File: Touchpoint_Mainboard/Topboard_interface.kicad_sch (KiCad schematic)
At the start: 1 part, among them J3 Conn_01x10

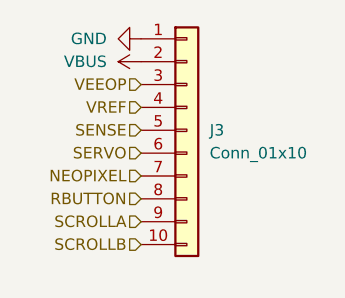
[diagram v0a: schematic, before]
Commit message: FInished populating mainboard schematic
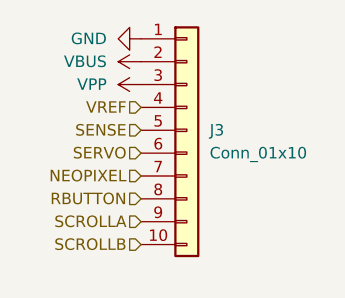
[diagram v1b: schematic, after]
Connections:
- net VEEOP renamed VPP
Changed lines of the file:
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@@
-		)
-	)
-	(hierarchical_label "VEEOP"
-		(shape input)
-		(at 52.07 43.18 180)
-		(effects
-			(font
-				(size 1.27 1.27)
-			)
-			(justify right)
 		)
 	)
@@
 					(unit 1)
 				)
+			)
+		)
+	)
+	(symbol
+		(lib_id "power:VPP")
+		(at 52.07 43.18 90)
+		(unit 1)
+		(exclude_from_sim no)
+		(in_bom yes)
+		(on_board yes)
+		(dnp no)
+		(fields_autoplaced yes)
+		(property "Reference" "#PWR081"
+			(at 55.88 43.18 0)
+			(effects
+				(font
+					(size 1.27 1.27)
+				)
+				(hide yes)
+			)
+		)
+		(property "Value" "VPP"
+			(at 48.26 43.1799 90)
+			(effects
+				(font
+					(size 1.27 1.27)
+				)
+				(justify left)
+			)
+		)
+		(property "Footprint" ""
+			(at 52.07 43.18 0)
+			(effects
+				(font
+					(size 1.27 1.27)
+				)
+				(hide yes)
+			)
+		)
+		(property "Datasheet" ""
+			(at 52.07 43.18 0)
+			(effects
+				(font
+					(size 1.27 1.27)
+				)
+				(hide yes)
+			)
+		)
+		(property "Description" "Power symbol creates a global label with name \"VPP\""
+			(at 52.07 43.18 0)
+			(effects
+				(font
+					(size 1.27 1.27)
+				)
+				(hide yes)
+			)
+		)
+		(pin "1"
+		)
+		(instances
+			(project "Touchpoint_Mainboard"
+				(path "/f37b5f88-420a-4646-85df-8f9851d23e3c/3f8a48d9-15ab-478a-aaa5-794276ddae05"
+					(reference "#PWR081")
+					(unit 1)
+				)

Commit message: Added remaining interface things to topboard schematic
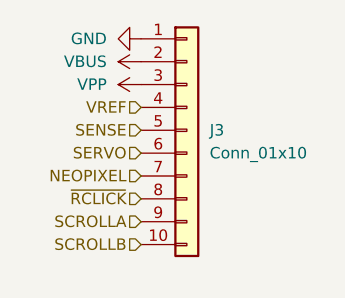
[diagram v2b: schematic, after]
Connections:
- net RBUTTON renamed ~{RCLICK}
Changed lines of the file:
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@@
 		)
 	)
-	(hierarchical_label "RBUTTON"
+	(hierarchical_label "~{RCLICK}"
 		(shape input)
 		(at 52.07 55.88 180)

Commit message: Finished assigning most footprints
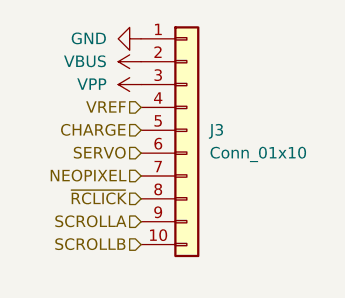
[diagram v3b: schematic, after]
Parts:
- J3: footprint (none) -> Connector_PinHeader_2.54mm:PinHeader_1x10_P2.54mm_Vertical
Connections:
- net SENSE renamed CHARGE
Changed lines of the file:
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@@
 		)
 	)
-	(hierarchical_label "SENSE"
+	(hierarchical_label "CHARGE"
 		(shape input)
 		(at 52.07 48.26 180)
@@
 			)
 		)
-		(property "Footprint" ""
+		(property "Footprint" "Connector_PinHeader_2.54mm:PinHeader_1x10_P2.54mm_Vertical"
 			(at 57.15 48.26 0)
 			(effects

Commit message: Changed to jumper connector between boards
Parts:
- J3: footprint Connector_PinHeader_2.54mm:PinHeader_1x10_P2.54mm_Vertical -> Touchpoint:Jumper_Interface_10
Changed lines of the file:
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@@
 			)
 		)
-		(property "Footprint" "Connector_PinHeader_2.54mm:PinHeader_1x10_P2.54mm_Vertical"
+		(property "Footprint" "Touchpoint:Jumper_Interface_10"
 			(at 57.15 48.26 0)
 			(effects

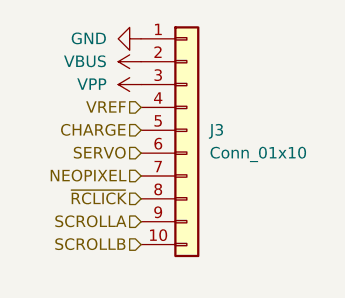
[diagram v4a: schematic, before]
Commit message: Added 3.3V to interface
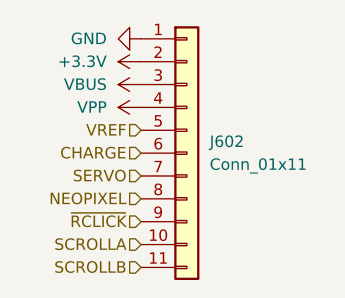
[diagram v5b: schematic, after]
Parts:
- removed J3: Conn_01x10, Touchpoint:Jumper_Interface_10, symbol Connector_Generic:Conn_01x10
- added J602: Conn_01x11, Touchpoint:Jumper_Interface_11, symbol Connector_Generic:Conn_01x11
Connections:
- net CHARGE: now also J602.6 (Pin_6)
- net GND: now also J602.1 (Pin_1)
- net NEOPIXEL: now also J602.8 (Pin_8)
- net SCROLLA: now also J602.10 (Pin_10)
- net SCROLLB: now also J602.11 (Pin_11)
- net SERVO: now also J602.7 (Pin_7)
- net VBUS: now also J602.3 (Pin_3)
- net VPP: now also J602.4 (Pin_4)
- net VREF: now also J602.5 (Pin_5)
- net ~{RCLICK}: now also J602.9 (Pin_9)
- new net +3.3V: J602.2 (Pin_2)
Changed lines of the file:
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@@
 	(hierarchical_label "SCROLLA"
 		(shape input)
+		(at 52.07 60.96 180)
+		(effects
+			(font
+				(size 1.27 1.27)
+			)
+			(justify right)
+		)
+	)
+	(hierarchical_label "VREF"
+		(shape input)
+		(at 52.07 48.26 180)
+		(effects
+			(font
+				(size 1.27 1.27)
+			)
+			(justify right)
+		)
+	)
+	(hierarchical_label "SERVO"
+		(shape input)
+		(at 52.07 53.34 180)
+		(effects
+			(font
+				(size 1.27 1.27)
+			)
+			(justify right)
+		)
+	)
+	(hierarchical_label "~{RCLICK}"
+		(shape input)
 		(at 52.07 58.42 180)
 		(effects
@@
 		)
 	)
-	(hierarchical_label "VREF"
-		(shape input)
-		(at 52.07 45.72 180)
-		(effects
-			(font
-				(size 1.27 1.27)
-			)
-			(justify right)
-		)
-	)
-	(hierarchical_label "SERVO"
+	(hierarchical_label "SCROLLB"
+		(shape input)
+		(at 52.07 63.5 180)
+		(effects
+			(font
+				(size 1.27 1.27)
+			)
+			(justify right)
+		)
+	)
+	(hierarchical_label "CHARGE"
 		(shape input)
 		(at 52.07 50.8 180)
@@
 		)
 	)
-	(hierarchical_label "~{RCLICK}"
+	(hierarchical_label "NEOPIXEL"
 		(shape input)
 		(at 52.07 55.88 180)
@@
 		)
 	)
-	(hierarchical_label "SCROLLB"
-		(shape input)
-		(at 52.07 60.96 180)
-		(effects
-			(font
-				(size 1.27 1.27)
-			)
-			(justify right)
-		)
-	)
-	(hierarchical_label "CHARGE"
-		(shape input)
-		(at 52.07 48.26 180)
-		(effects
-			(font
-				(size 1.27 1.27)
-			)
-			(justify right)
-		)
-	)
-	(hierarchical_label "NEOPIXEL"
-		(shape input)
-		(at 52.07 53.34 180)
-		(effects
-			(font
-				(size 1.27 1.27)
-			)
-			(justify right)
-		)
-	)
 	(symbol
-		(lib_id "Connector_Generic:Conn_01x10")
-		(at 57.15 48.26 0)
+		(lib_id "power:VBUS")
+		(at 52.07 43.18 90)
 		(unit 1)
 		(exclude_from_sim no)
@@
 		(dnp no)
 		(fields_autoplaced yes)
-		(property "Reference" "J3"
-			(at 59.69 48.2599 0)
+		(property "Reference" "#PWR0602"
+			(at 55.88 43.18 0)
+			(effects
+				(font
+					(size 1.27 1.27)
+				)
+				(hide yes)
+			)
+		)
+		(property "Value" "VBUS"
+			(at 48.26 43.1799 90)
 			(effects
 				(font
@@
 			)
 		)
-		(property "Value" "Conn_01x10"
-			(at 59.69 50.7999 0)
-			(effects
-				(font
-					(size 1.27 1.27)
-				)
-				(justify left)
-			)
-		)
-		(property "Footprint" "Touchpoint:Jumper_Interface_10"
-			(at 57.15 48.26 0)
-			(effects
-				(font
-					(size 1.27 1.27)
-				)
-				(hide yes)
-			)
-		)
-		(property "Datasheet" "~"
-			(at 57.15 48.26 0)
-			(effects
-				(font
-					(size 1.27 1.27)
-				)
-				(hide yes)
-			)
-		)
-		(property "Description" "Generic connector, single row, 01x10, script generated (kicad-library-utils/schlib/autogen/connector/)"
-			(at 57.15 48.26 0)
+		(property "Footprint" ""
+			(at 52.07 43.18 0)
+			(effects
+				(font
+					(size 1.27 1.27)
+				)
+				(hide yes)
+			)
+		)
+		(property "Datasheet" ""
+			(at 52.07 43.18 0)
+			(effects
+				(font
+					(size 1.27 1.27)
+				)
+				(hide yes)
+			)
+		)
+		(property "Description" "Power symbol creates a global label with name \"VBUS\""
+			(at 52.07 43.18 0)
 			(effects
 				(font
@@
 		)
 		(pin "1"
-		)
-		(pin "2"
-		)
-		(pin "3"
-		)
-		(pin "4"
-		)
-		(pin "5"
-		)
-		(pin "7"
-		)
-		(pin "9"
-		)
-		(pin "6"
-		)
-		(pin "8"
-		)
-		(pin "10"
 		)
 		(instances
 			(project ""
 				(path "/f37b5f88-420a-4646-85df-8f9851d23e3c/3f8a48d9-15ab-478a-aaa5-794276ddae05"
-					(reference "J3")
+					(reference "#PWR0602")
 					(unit 1)
 				)
@@
 	)
 	(symbol
-		(lib_id "power:VBUS")
+		(lib_id "power:+3.3V")
 		(at 52.07 40.64 90)
 		(unit 1)
@@
 		(dnp no)
 		(fields_autoplaced yes)
-		(property "Reference" "#PWR074"
+		(property "Reference" "#PWR0604"
 			(at 55.88 40.64 0)
 			(effects
@@
 			)
 		)
-		(property "Value" "VBUS"
+		(property "Value" "+3.3V"
 			(at 48.26 40.6399 90)
 			(effects
@@
 			)
 		)
-		(property "Description" "Power symbol creates a global label with name \"VBUS\""
+		(property "Description" "Power symbol creates a global label with name \"+3.3V\""
 			(at 52.07 40.64 0)
 			(effects
@@
 			(project ""
 				(path "/f37b5f88-420a-4646-85df-8f9851d23e3c/3f8a48d9-15ab-478a-aaa5-794276ddae05"
-					(reference "#PWR074")
+					(reference "#PWR0604")
 					(unit 1)
 				)
@@
 	(symbol
 		(lib_id "power:VPP")
-		(at 52.07 43.18 90)
+		(at 52.07 45.72 90)
 		(unit 1)
 		(exclude_from_sim no)
@@
 		(dnp no)
 		(fields_autoplaced yes)
-		(property "Reference" "#PWR081"
-			(at 55.88 43.18 0)
+		(property "Reference" "#PWR0603"
+			(at 55.88 45.72 0)
 			(effects
 				(font
@@
 		)
 		(property "Value" "VPP"
-			(at 48.26 43.1799 90)
+			(at 48.26 45.7199 90)
 			(effects
 				(font
@@
 		)
 		(property "Footprint" ""
-			(at 52.07 43.18 0)
+			(at 52.07 45.72 0)
 			(effects
 				(font
@@
 		)
 		(property "Datasheet" ""
-			(at 52.07 43.18 0)
+			(at 52.07 45.72 0)
 			(effects
 				(font
@@
 		)
 		(property "Description" "Power symbol creates a global label with name \"VPP\""
-			(at 52.07 43.18 0)
+			(at 52.07 45.72 0)
 			(effects
 				(font
@@
 			(project "Touchpoint_Mainboard"
 				(path "/f37b5f88-420a-4646-85df-8f9851d23e3c/3f8a48d9-15ab-478a-aaa5-794276ddae05"
-					(reference "#PWR081")
+					(reference "#PWR0603")
 					(unit 1)
 				)
@@
 		(dnp no)
 		(fields_autoplaced yes)
-		(property "Reference" "#PWR075"
+		(property "Reference" "#PWR0601"
 			(at 45.72 38.1 0)
 			(effects
@@
 			(project ""
 				(path "/f37b5f88-420a-4646-85df-8f9851d23e3c/3f8a48d9-15ab-478a-aaa5-794276ddae05"
-					(reference "#PWR075")
+					(reference "#PWR0601")
 					(unit 1)
 				)
+			)
+		)
+	)
+	(symbol
+		(lib_id "Connector_Generic:Conn_01x11")
+		(at 57.15 50.8 0)
+		(unit 1)
+		(exclude_from_sim no)
+		(in_bom yes)
+		(on_board yes)
+		(dnp no)
+		(fields_autoplaced yes)
+		(property "Reference" "J602"
+			(at 59.69 49.5299 0)
+			(effects
+				(font
+					(size 1.27 1.27)
+				)
+				(justify left)
+			)
+		)
+		(property "Value" "Conn_01x11"
+			(at 59.69 52.0699 0)
+			(effects
+				(font
+					(size 1.27 1.27)
+				)
+				(justify left)
+			)
+		)
+		(property "Footprint" "Touchpoint:Jumper_Interface_11"
+			(at 57.15 50.8 0)
+			(effects
+				(font
+					(size 1.27 1.27)
+				)
+				(hide yes)
+			)
+		)
+		(property "Datasheet" "~"
+			(at 57.15 50.8 0)
+			(effects
+				(font
+					(size 1.27 1.27)
+				)
+				(hide yes)
+			)
+		)
+		(property "Description" "Generic connector, single row, 01x11, script generated (kicad-library-utils/schlib/autogen/connector/)"
+			(at 57.15 50.8 0)
+			(effects
+				(font
+					(size 1.27 1.27)
+				)
+				(hide yes)
+			)
+		)
+		(pin "5"
+		)
+		(pin "1"
+		)
+		(pin "2"
+		)
+		(pin "3"
+		)
+		(pin "4"
+		)
+		(pin "7"
+		)
+		(pin "11"
+		)
+		(pin "6"
+		)
+		(pin "8"
+		)
+		(pin "9"
+		)
+		(pin "10"
+		)
+		(instances
+			(project ""
+				(path "/f37b5f88-420a-4646-85df-8f9851d23e3c/3f8a48d9-15ab-478a-aaa5-794276ddae05"
+					(reference "J602")
+					(unit 1)
+				)

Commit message: Final manufacturing adjustments
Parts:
- removed J602: Conn_01x11, Touchpoint:Jumper_Interface_11, symbol Connector_Generic:Conn_01x11
- added J602: Conn_01x10, Touchpoint:Jumper_Interface_10, symbol Connector_Generic:Conn_01x10
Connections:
- net CHARGE: now also J602.5 (Pin_5)
- net GND: now also J602.1 (Pin_1)
- net NEOPIXEL: now also J602.7 (Pin_7)
- net SCROLLA: now also J602.9 (Pin_9)
- net SCROLLB: now also J602.10 (Pin_10)
- net SERVO: now also J602.6 (Pin_6)
- net VBUS: now also J602.2 (Pin_2)
- net VPP: now also J602.3 (Pin_3)
- net VREF: now also J602.4 (Pin_4)
- net ~{RCLICK}: now also J602.8 (Pin_8)
